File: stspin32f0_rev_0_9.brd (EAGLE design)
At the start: 75 x 48 mm, 83 parts, among them IC1 STSPIN32F0, J1 2X6 FEMALE, Q1 IPD088N06N3_G, Q2 IPD088N06N3_G, Q3 IPD088N06N3_G, Q4 IPD088N06N3_G, Q5 IPD088N06N3_G, Q6 IPD088N06N3_G

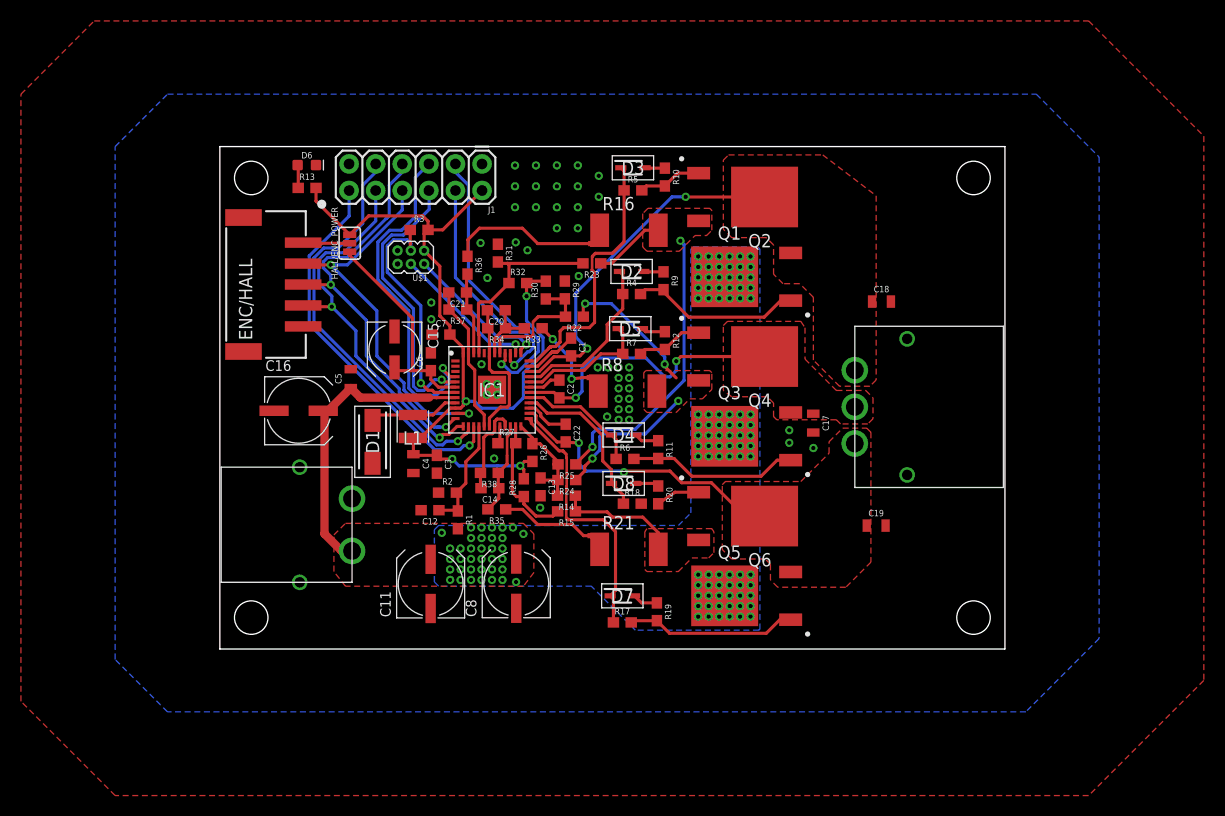
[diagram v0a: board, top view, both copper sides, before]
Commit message: routing done and drc cleared
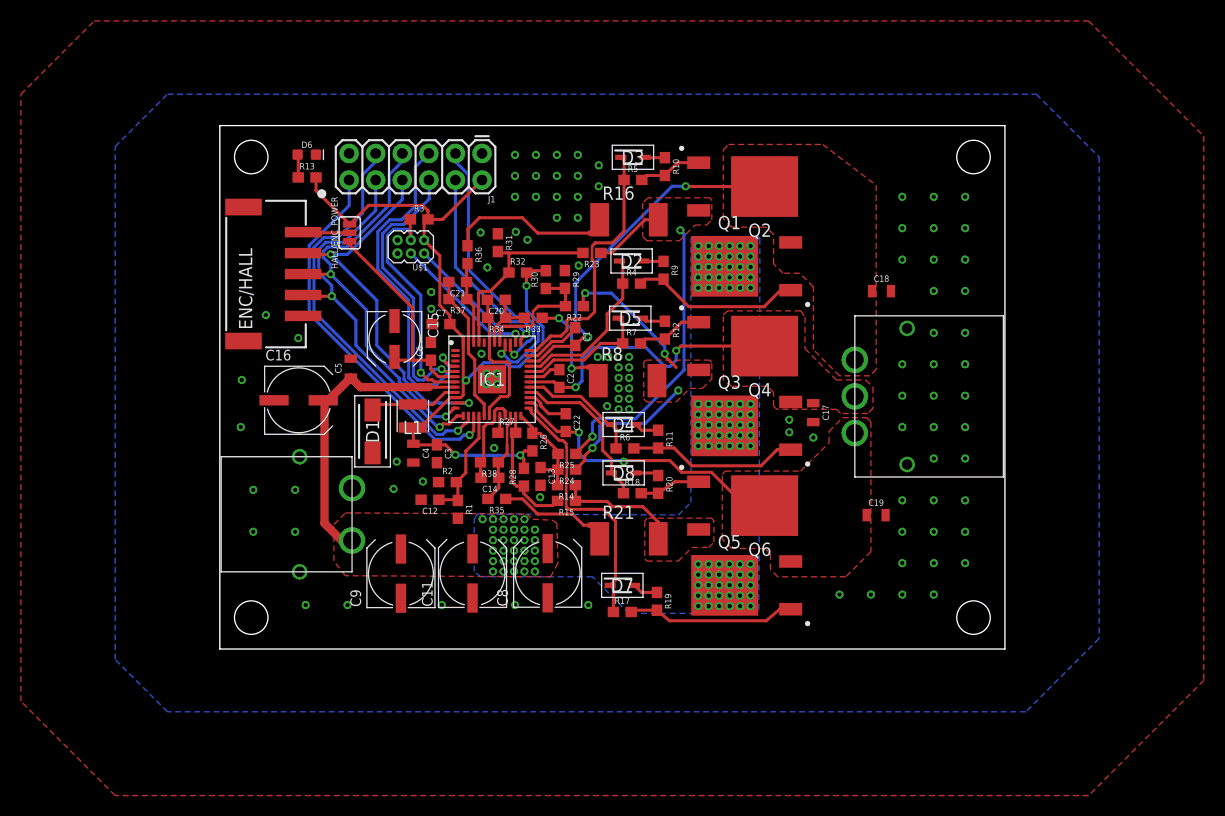
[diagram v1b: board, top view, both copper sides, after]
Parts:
- added C9: 100uF, rcl:UD-6,3X7,7_NICHICON
- moved C11 4.12 mm to (24.1, 7.22)
- moved C8 3.16 mm to (31.3, 7.24)
- moved C1 1.08 mm to (34.0, 29.9)
- moved D8 1.00 mm to (38.6, 16.8)
- moved C12 1.00 mm to (20.1, 14.3)
- moved C14 1.00 mm to (25.8, 16.4)
- moved C15 1.00 mm to (16.7, 29.6)
- moved C16 1.00 mm to (7.53, 23.8)
- moved C17 1.00 mm to (56.7, 22.6)
- moved C18 1.00 mm to (63.2, 34.2)
- moved C19 1.00 mm to (62.7, 12.8)
- moved C2 1.00 mm to (32.4, 25.8)
- moved C20 1.00 mm to (26.4, 33.4)
- moved C21 1.00 mm to (22.7, 35.1)
- moved C22 1.00 mm to (33.0, 21.6)
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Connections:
- net GND: now also C9.-
- net V_BATT: now also C9.+
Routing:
- net N$10: track 4.20 -> 5.83 mm
- net 3.3V: track 82.1 -> 80.5 mm
- net IB_SENSE_N: track 7.51 -> 8.56 mm
- net ENC_B/HALL2: track 39.3 -> 38.7 mm
- net ENC_A/HALL1: track 37.3 -> 36.8 mm
- net V_BATT: vias 126 -> 120
- net GND: vias 48 -> 101
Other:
- board size 75 x 48 mm -> 75 x 50 mm

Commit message: minor fixes
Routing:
- net GND: vias 101 -> 120
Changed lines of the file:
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@@
 <via x="21.2" y="4.2" extent="1-16" drill="0.4" diameter="0.8"/>
 <via x="28.2" y="4.2" extent="1-16" drill="0.4" diameter="0.8"/>
-<via x="35.2" y="4.2" extent="1-16" drill="0.4" diameter="0.8"/>
+<via x="28.2" y="2.2" extent="1-16" drill="0.4" diameter="0.8"/>
 <via x="4.4" y="31.9" extent="1-16" drill="0.4" diameter="0.8"/>
 <via x="7.5" y="29.7" extent="1-16" drill="0.4" diameter="0.8"/>
 <via x="2.1" y="25.7" extent="1-16" drill="0.4" diameter="0.8"/>
 <via x="2" y="21.2" extent="1-16" drill="0.4" diameter="0.8"/>
+<via x="32.8" y="6.1" extent="1-16" drill="0.4" diameter="0.8"/>
+<via x="33.8" y="6.1" extent="1-16" drill="0.4" diameter="0.8"/>
+<via x="34.8" y="6.1" extent="1-16" drill="0.4" diameter="0.8"/>
+<via x="35.8" y="5.1" extent="1-16" drill="0.4" diameter="0.8"/>
+<via x="32.8" y="5.1" extent="1-16" drill="0.4" diameter="0.8"/>
+<via x="33.8" y="5.1" extent="1-16" drill="0.4" diameter="0.8"/>
+<via x="34.8" y="5.1" extent="1-16" drill="0.4" diameter="0.8"/>
+<via x="32.8" y="4.1" extent="1-16" drill="0.4" diameter="0.8"/>
+<via x="33.8" y="4.1" extent="1-16" drill="0.4" diameter="0.8"/>
+<via x="34.8" y="4.1" extent="1-16" drill="0.4" diameter="0.8"/>
+<via x="34.8" y="3.1" extent="1-16" drill="0.4" diameter="0.8"/>
+<via x="33.8" y="3.1" extent="1-16" drill="0.4" diameter="0.8"/>
+<via x="32.8" y="3.1" extent="1-16" drill="0.4" diameter="0.8"/>
+<via x="35.8" y="4.1" extent="1-16" drill="0.4" diameter="0.8"/>
+<via x="35.8" y="3.1" extent="1-16" drill="0.4" diameter="0.8"/>
+<via x="35.8" y="2.1" extent="1-16" drill="0.4" diameter="0.8"/>
+<via x="34.8" y="2.1" extent="1-16" drill="0.4" diameter="0.8"/>
+<via x="33.8" y="2.1" extent="1-16" drill="0.4" diameter="0.8"/>
+<via x="32.8" y="2.1" extent="1-16" drill="0.4" diameter="0.8"/>
 </signal>
 <signal name="V_BATT">

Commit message: fixed names
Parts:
- renumbered J1 to IO, U$1 to PROG
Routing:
- net GND: track 6.79 -> 8.90 mm
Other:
- board text added: "+"
- board text added: "-"
- board text added: "12v"
- board text added: "3.3V"
- board text added: "8-45V input"
- board text added: "BESC v0.9"
- board text added: "Designed by Ole Bauck 7/2017"
- board text added: "Max 30A"
- board text added: "Motor out"
- board text added: "U"
- board text added: "V"
- board text added: "W"

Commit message: More vias and wider tracks for more current
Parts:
- moved R22 0.80 mm to (33.9, 33.5)
- moved R29 0.71 mm to (32.9, 36.0)
- moved R30 0.70 mm to (31.1, 36.0)
- moved R32 0.50 mm to (28.5, 36.5)
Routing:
- net IB_SENSE_N: track 8.56 -> 11.2 mm
- net 3.3V: track 80.5 -> 81.1 mm
- net GND: vias 120 -> 166
